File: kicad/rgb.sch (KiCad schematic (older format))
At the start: 25 parts, among them J1 1935776, J2 Conn_01x05, J3 Conn_01x05, J4 Conn_01x04, J5 Conn_01x02, Q1 DMG9926USD, Q2 DMG9926USD, Q3 DMG9926USD, Q4 DMG9926USD, SW1 SW_Push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

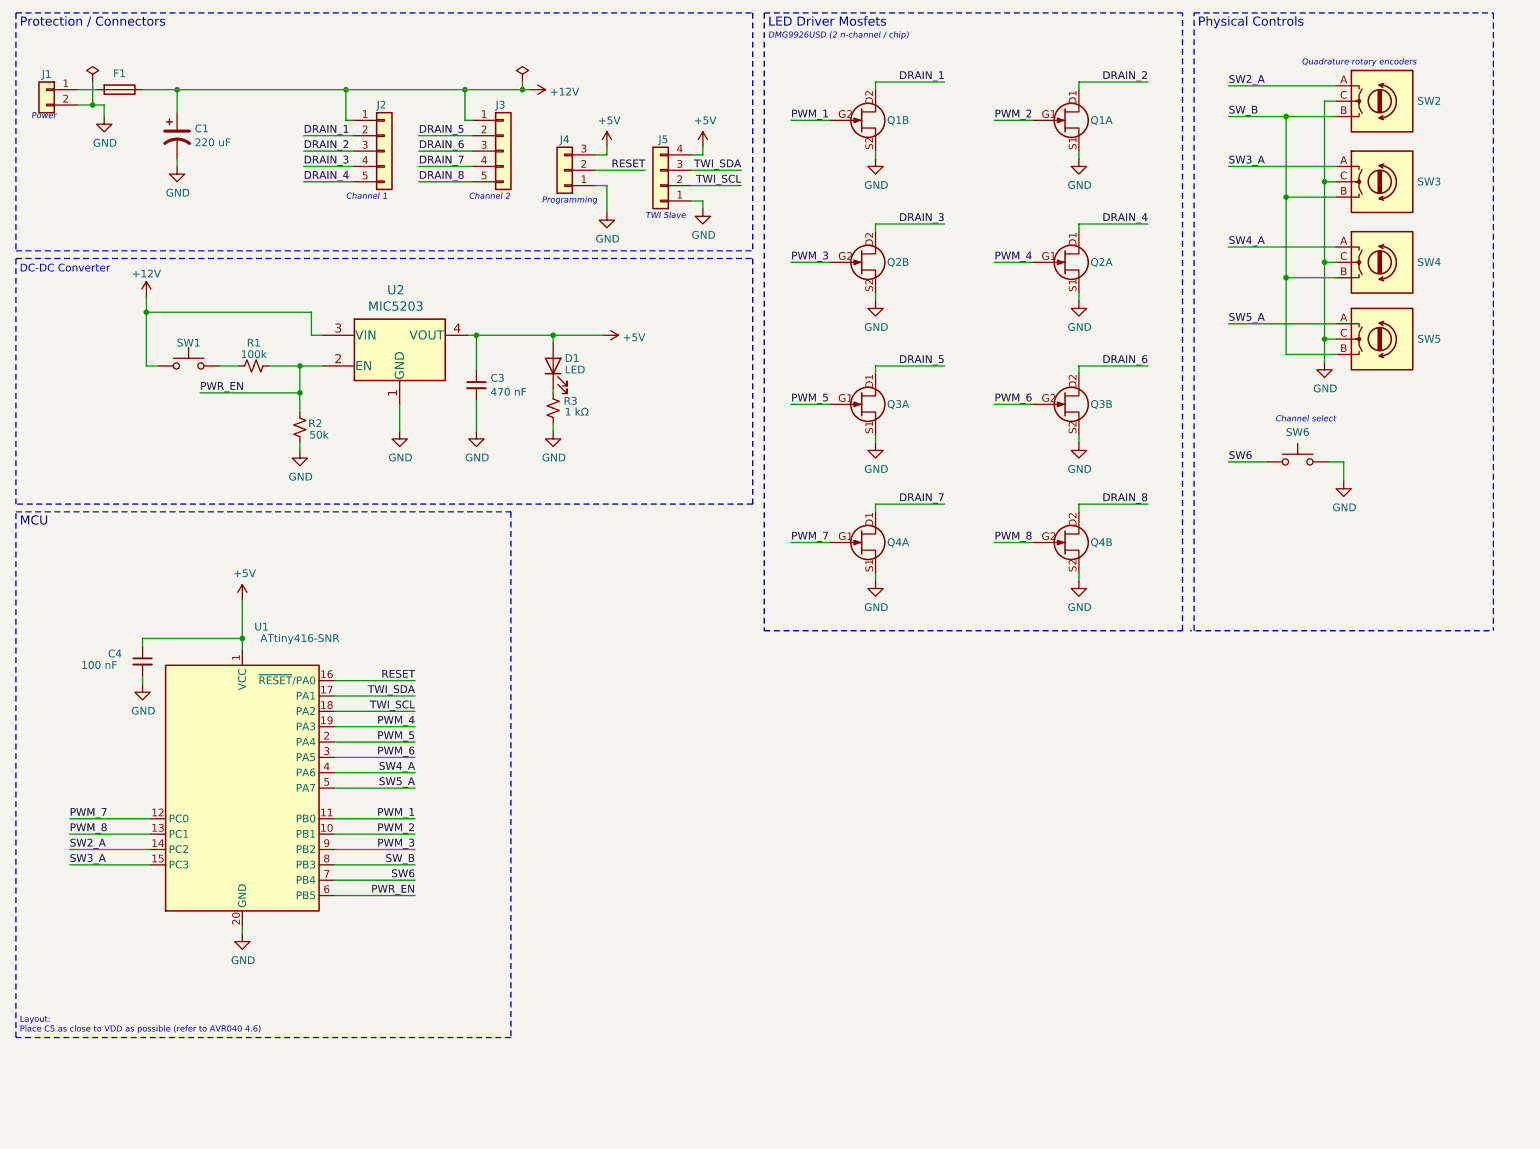
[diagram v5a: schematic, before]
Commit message: more power planes
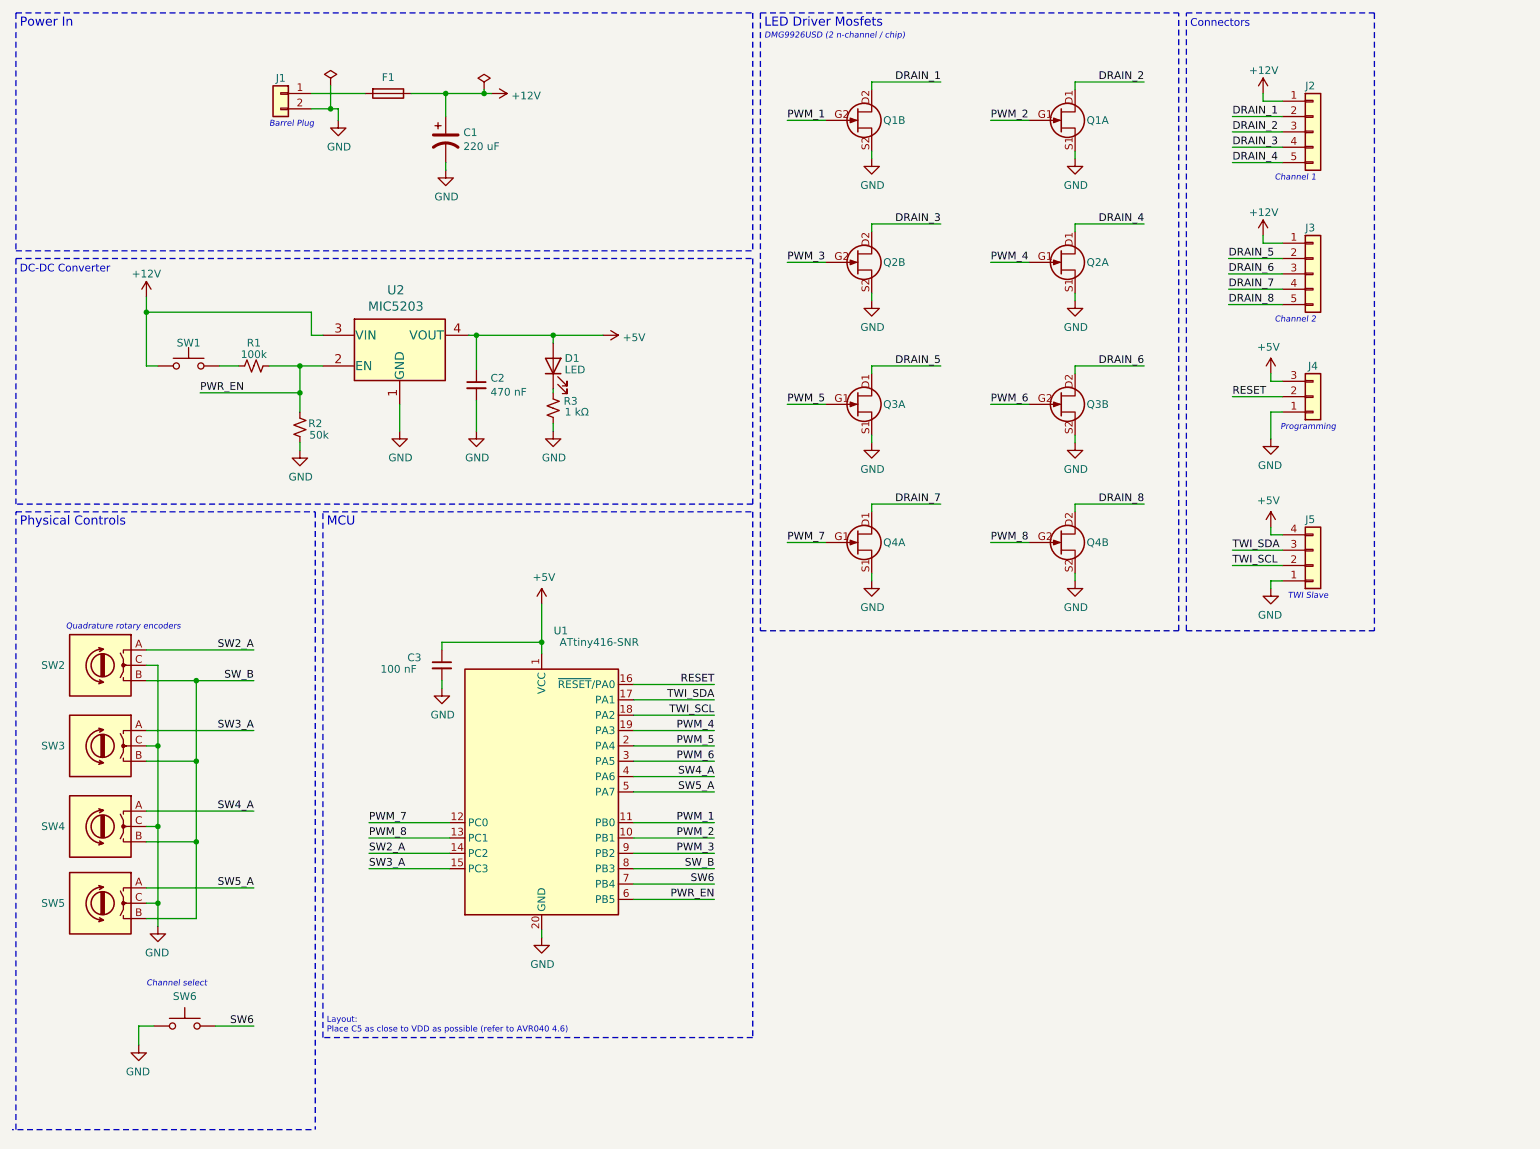
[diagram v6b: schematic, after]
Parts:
- renumbered C3 to C2, C4 to C3
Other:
- note added: "Barrel Plug"
- note added: "Connectors\n"
- note added: "Power In"
- note removed: "Power"
- note removed: "Protection / Connectors\n"
- moved on the sheet: C1, C3, F1, J1, J2, J3, J4, J5, Q1A, Q1B, Q2A, Q2B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

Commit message: trace routing
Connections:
- net +12V: now also R1.2; no longer SW1.2
- net GND: now also SW6.2; no longer SW6.1
- net PWM_1: now also U1.12 (PC0); no longer U1.11 (PB0)
- net PWM_2: now also U1.11 (PB0); no longer U1.10 (PB1)
- net PWM_3: now also U1.13 (PC1); no longer U1.9 (PB2)
- net PWM_7: now also U1.10 (PB1); no longer U1.12 (PC0)
- net PWM_8: now also U1.9 (PB2); no longer U1.13 (PC1)
- net PWR_EN: now also SW1.2; no longer R1.1
- net SW2_A: now also U1.5 (PA7); no longer U1.14 (PC2)
- net SW5_A: now also U1.14 (PC2); no longer U1.5 (PA7)
- net SW6: now also SW6.1; no longer SW6.2
- net at SW1.1: now also R1.1; no longer R1.2
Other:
- moved on the sheet: R1, SW1
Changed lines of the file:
@@
 F 3 "~" H 1650 7350 50  0001 C CNN
 	1    1650 7150
-	1    0    0    -1
+	-1   0    0    -1
 $EndComp
 Wire Wire Line
@@
 L Switch:SW_Push SW1
 U 1 1 5FF0425C
-P 1675 2850
-F 0 "SW1" H 1675 3000 50  0000 C CNN
-F 1 "SW_Push" H 1675 3044 50  0001 C CNN
-F 2 "Button_Switch_THT:SW_PUSH_6mm_H13mm" H 1675 3050 50  0001 C CNN
-F 3 "~" H 1675 3050 50  0001 C CNN
-	1    1675 2850
-	-1   0    0    -1
+P 2000 2850
+F 0 "SW1" H 2000 3000 50  0000 C CNN
+F 1 "SW_Push" H 2000 3044 50  0001 C CNN
+F 2 "Button_Switch_THT:SW_PUSH_6mm_H13mm" H 2000 3050 50  0001 C CNN
+F 3 "~" H 2000 3050 50  0001 C CNN
+	1    2000 2850
+	1    0    0    -1
 $EndComp
 $Comp
@@
 $EndComp
 Wire Wire Line
-	1400 2850 1475 2850
-Wire Wire Line
-	1875 2850 2000 2850
-Wire Wire Line
 	3050 3100 3050 3275
 Text Label 1750 3025 0    50   ~ 0
@@
 $EndComp
 $Comp
-L Device:R_Small_US R1
-U 1 1 5FF53AFE
-P 2100 2850
-F 0 "R1" V 1950 2850 50  0000 C CNN
-F 1 "100k" V 2025 2850 50  0000 C CNN
-F 2 "Resistor_SMD:R_0603_1608Metric_Pad1.05x0.95mm_HandSolder" H 2100 2850 50  0001 C CNN
-F 3 "~" H 2100 2850 50  0001 C CNN
-	1    2100 2850
-	0    1    1    0
-$EndComp
-$Comp
 L power:+12V #PWR0103
 U 1 1 6001ACE1
@@
 Wire Wire Line
 	4575 4925 5100 4925
-Text Label 5100 5425 2    50   ~ 0
-PWM_6
 Wire Wire Line
 	4575 5425 5100 5425
-Text Label 5100 5325 2    50   ~ 0
-PWM_5
 Wire Wire Line
 	4575 5325 5100 5325
@@
 Wire Wire Line
 	4575 5025 5100 5025
-Text Label 5100 5625 2    50   ~ 0
+Text Label 2850 6025 0    50   ~ 0
 SW5_A
 Wire Wire Line
@@
 Wire Wire Line
 	4575 5525 5100 5525
-Text Label 2850 6025 0    50   ~ 0
+Text Label 5100 5625 2    50   ~ 0
 SW2_A
 Wire Wire Line
@@
 Wire Wire Line
 	4575 6125 5100 6125
-Text Label 5100 6025 2    50   ~ 0
+Text Label 2850 5925 0    50   ~ 0
 PWM_3
 Wire Wire Line
@@
 	1    0    0    -1
 $EndComp
-Text Label 5100 5825 2    50   ~ 0
-PWM_1
 Wire Wire Line
 	4575 5825 5100 5825
+Wire Wire Line
+	4575 5925 5100 5925
 Text Label 5100 5925 2    50   ~ 0
-PWM_2
-Wire Wire Line
-	4575 5925 5100 5925
-Text Label 2850 5825 0    50   ~ 0
 PWM_7
 Wire Wire Line
 	3375 5825 2850 5825
-Text Label 2850 5925 0    50   ~ 0
+Text Label 5100 6025 2    50   ~ 0
 PWM_8
 Wire Wire Line
@@
 Wire Notes Line
 	8175 4575 9400 4575
+$Comp
+L Device:R_Small_US R1
+U 1 1 5FF53AFE
+P 1600 2850
+F 0 "R1" V 1450 2850 50  0000 C CNN
+F 1 "100k" V 1525 2850 50  0000 C CNN
+F 2 "Resistor_SMD:R_0603_1608Metric_Pad1.05x0.95mm_HandSolder" H 1600 2850 50  0001 C CNN
+F 3 "~" H 1600 2850 50  0001 C CNN
+	1    1600 2850
+	0    1    1    0
+$EndComp
+Wire Wire Line
+	1400 2850 1500 2850
+Wire Wire Line
+	1700 2850 1800 2850
+Text Label 5100 5425 2    50   ~ 0
+PWM_6
+Text Label 5100 5325 2    50   ~ 0
+PWM_5
+Text Label 2850 5825 0    50   ~ 0
+PWM_1
+Text Label 5100 5825 2    50   ~ 0
+PWM_2
 $EndSCHEMATC

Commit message: pcb layout + mounting
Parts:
- C2: footprint Capacitor_SMD:C_0805_2012Metric_Pad1.15x1.40mm_HandSolder -> Capacitor_SMD:C_0603_1608Metric_Pad1.08x0.95mm_HandSolder
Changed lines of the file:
@@
 F 0 "C2" H 3642 3021 50  0000 L CNN
 F 1 "470 nF" H 3642 2930 50  0000 L CNN
-F 2 "Capacitor_SMD:C_0805_2012Metric_Pad1.15x1.40mm_HandSolder" H 3550 2975 50  0001 C CNN
+F 2 "Capacitor_SMD:C_0603_1608Metric_Pad1.08x0.95mm_HandSolder" H 3550 2975 50  0001 C CNN
 F 3 "~" H 3550 2975 50  0001 C CNN
 	1    3550 2975
